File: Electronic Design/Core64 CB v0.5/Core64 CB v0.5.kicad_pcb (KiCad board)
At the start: 2 copper layers, 85 x 85 mm, 36 parts, among them J1 TSM-116-03-T-SV‎, J2 TSM-116-03-T-SV‎, U1 SI7210-B-01, U2 SI7210-B-02, U3 SI7210-B-03, U4 SI7210-B-04, U5 LTR-329ALS-01, U6 TS3A4751PWR, U7 TS3A4751PWR, X1 SFH11-NBPC-D03-ST-BK

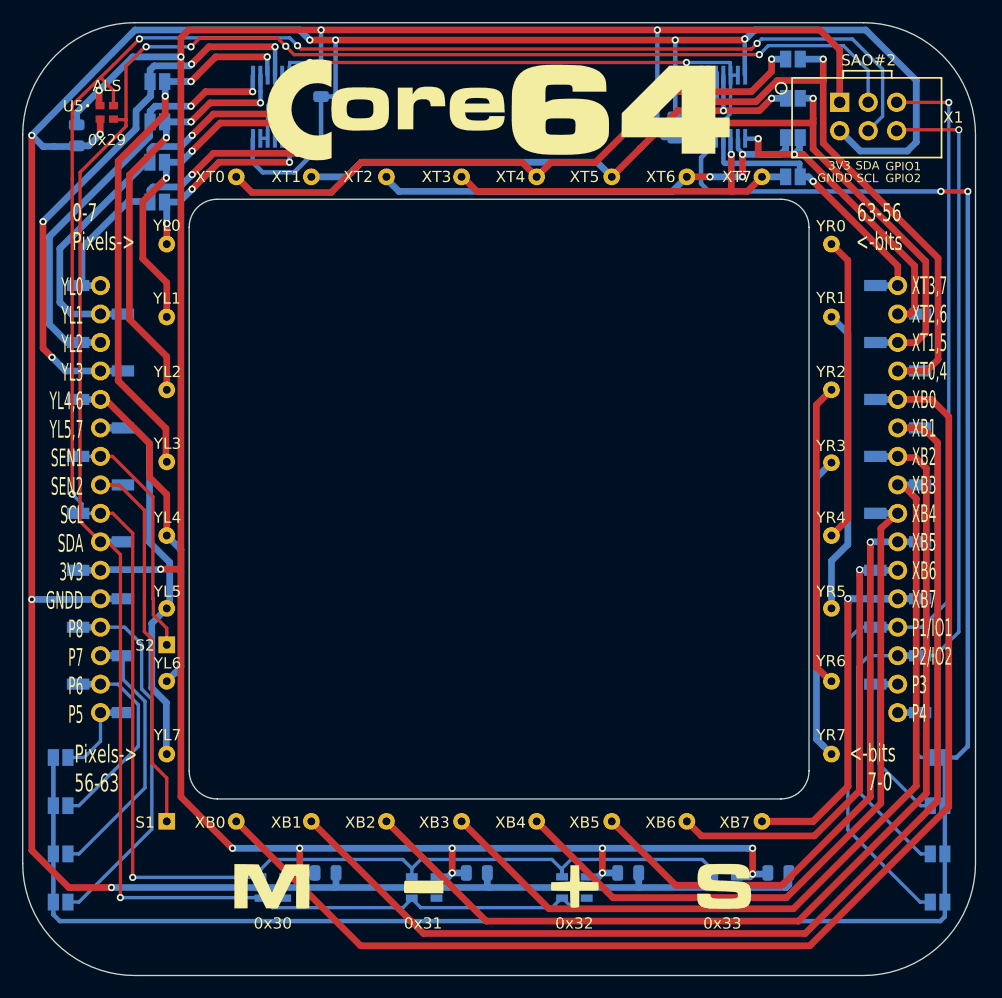
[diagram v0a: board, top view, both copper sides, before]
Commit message: Core board redline refinement
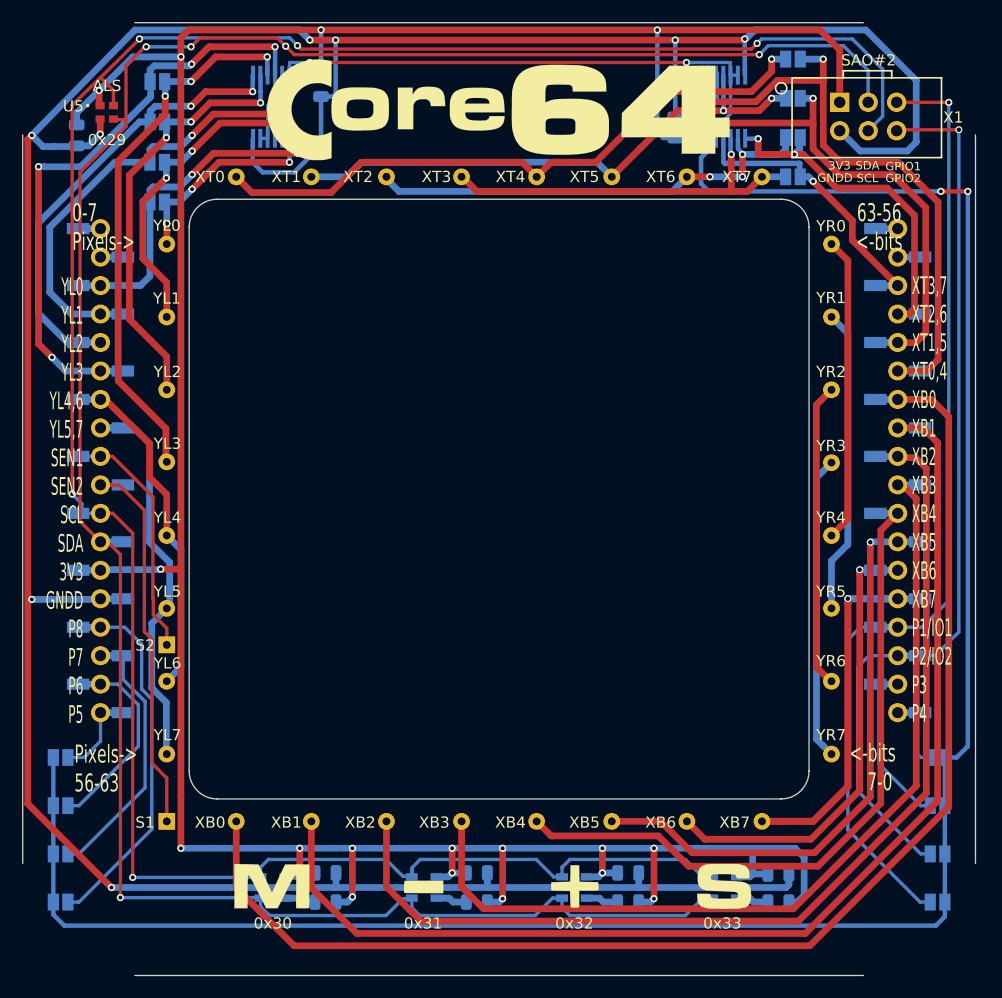
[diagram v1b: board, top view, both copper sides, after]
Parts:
- added R1: 10K, Resistor_SMD:R_0805_2012Metric, B.Cu at (-15.5, 36.0)
- added R2: 10K, Resistor_SMD:R_0805_2012Metric, B.Cu at (-1.99, 36.0)
- added R3: 10K, Resistor_SMD:R_0805_2012Metric, B.Cu at (11.5, 36.0)
- added R4: 10K, Resistor_SMD:R_0805_2012Metric, B.Cu at (24.9, 36.0)
- C5: value 1uF -> 0.1uF
- J1, J2: value TSM-116-03-T-SV‎ -> Digi-Key 77311-420-36LF-ND; footprint Connector_PinHeader_2.54mm:PinHeader_1x16_P2.54mm_Vertical_SMD_and_TH_Pin1Right -> Connector_PinHeader_2.54mm:PinHeader_1x18_P2.54mm_Vertical_SMD_and_TH_Pin1Right
- moved J1 5.08 mm to (-35.6, -5.08)
- moved J2 5.08 mm to (35.6, -5.08)
- moved C4 0.10 mm to (24.9, 33.5)
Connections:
- J1 pad 1: H_YL0 -> Net-(J1-Pad1)
- J1 pad 10: I2C_DATA -> SENSE1
- J1 pad 11: 3V3_800mA -> I2C_CLOCK
- J1 pad 12: GNDD -> I2C_DATA
- J1 pad 13: PLANE_8 -> 3V3_800mA
- J1 pad 14: PLANE_7 -> GNDD
- J1 pad 15: PLANE_6 -> PLANE_8
- J1 pad 16: PLANE_5 -> PLANE_7
- J1 pad 2: H_YL1 -> Net-(J1-Pad2)
- J1 pad 3: H_YL2 -> H_YL0
- J1 pad 4: H_YL3 -> H_YL1
- J1 pad 5: YL4 -> H_YL2
- J1 pad 6: YL5 -> H_YL3
- J1 pad 7: SENSE2 -> YL4
- J1 pad 8: SENSE1 -> YL5
- J1 pad 9: I2C_CLOCK -> SENSE2
- J2 pad 1: H_XT3-7 -> Net-(J2-Pad1)
- J2 pad 10: XB5 -> XB3
- J2 pad 11: XB6 -> XB4
- J2 pad 12: XB7 -> XB5
- J2 pad 13: PLANE_1 -> XB6
- J2 pad 14: PLANE_2 -> XB7
- J2 pad 15: PLANE_3 -> PLANE_1
- J2 pad 16: PLANE_4 -> PLANE_2
- J2 pad 2: H_XT2-6 -> Net-(J2-Pad2)
- J2 pad 3: H_XT1-5 -> H_XT3-7
- J2 pad 4: H_XT0-4 -> H_XT2-6
- J2 pad 5: XB0 -> H_XT1-5
- J2 pad 6: XB1 -> H_XT0-4
- J2 pad 7: XB2 -> XB0
- J2 pad 8: XB3 -> XB1
- J2 pad 9: XB4 -> XB2
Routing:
- net 3V3_800mA: track 248.0 -> 278.6 mm, vias 14 -> 18
- net XB1: track 102.7 -> 106.2 mm
- net XB0: track 114.9 -> 118.4 mm
- net XB2: track 90.2 -> 93.6 mm
- net XB3: track 77.8 -> 81.2 mm
- net I2C_DATA: track 207.5 -> 210.6 mm
- net H_XT0-4: track 53.2 -> 56.2 mm
- net Net-(R3-Pad2): track 0.00 -> 2.91 mm
- net Net-(R4-Pad2): track 0.00 -> 2.91 mm
- net H_XT1-5: track 44.9 -> 47.7 mm
- net Net-(R1-Pad2): track 0.00 -> 2.81 mm
- net Net-(R2-Pad2): track 0.00 -> 2.81 mm
- net H_YL1: track 38.4 -> 41.1 mm
- net H_XT2-6: track 29.4 -> 32.0 mm
- net H_YL3: track 51.1 -> 53.6 mm
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
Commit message: Update core grid to 6.75mm square
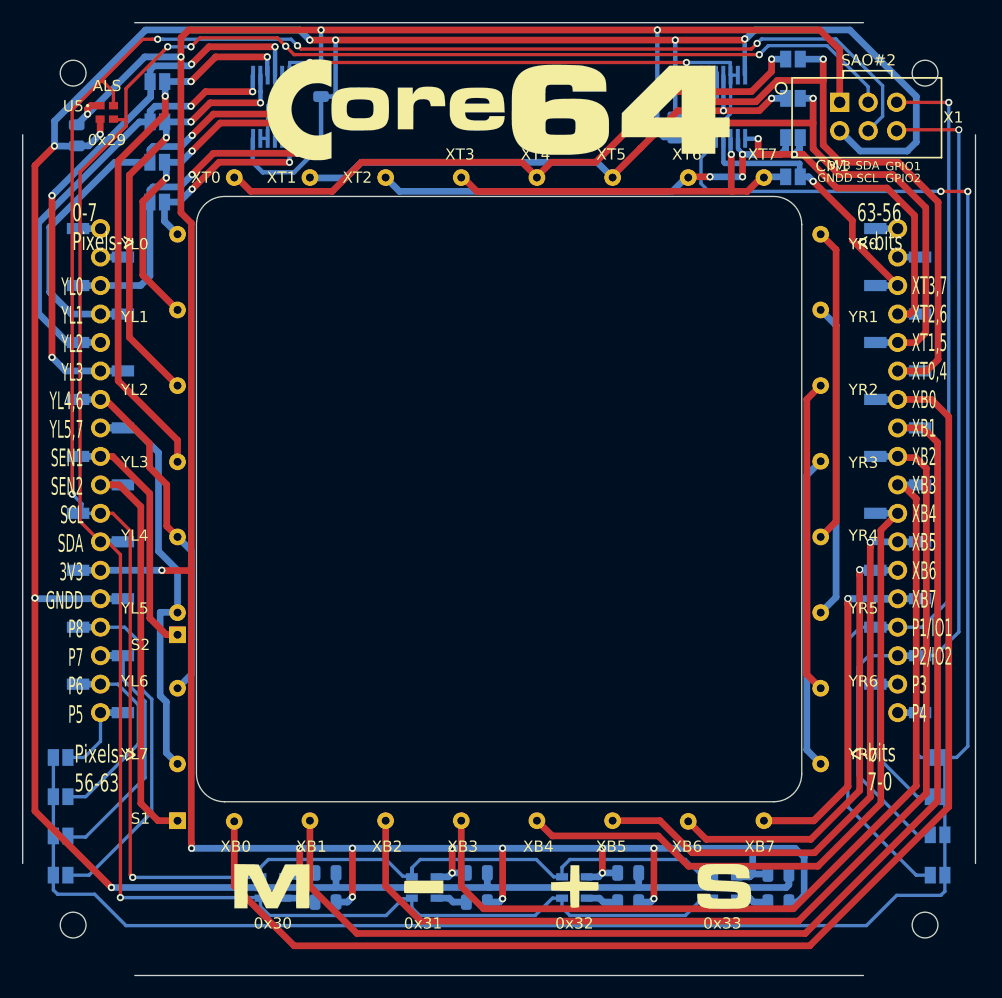
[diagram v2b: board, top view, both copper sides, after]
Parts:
- CM1: footprint Core_Memory_8x8_Array:core_64_x6.7_y6.5mm_v0.3_front_facing -> Core_Memory_8x8_Array:core_64_6.75mm_square_v0.5_front_facing
- moved JP16 2.40 mm to (-39.1, 33.5)
- moved JP9 2.40 mm to (39.1, 33.5)
- moved JP10 1.70 mm to (39.1, 29.9)
- moved JP15 1.60 mm to (-39.1, 30.1)
- moved JP11 0.80 mm to (39.1, 26.6)
- moved JP14 0.80 mm to (-39.1, 26.6)
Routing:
- net GNDD: track 281.0 -> 276.5 mm
- net H_YL3: track 53.6 -> 50.4 mm
- net ENABLE: track 245.4 -> 242.8 mm
- net PLANE_1: track 88.5 -> 86.3 mm
- net YL5: track 36.3 -> 38.4 mm
- net I2C_DATA: track 210.6 -> 208.6 mm
- net PLANE_8: track 35.0 -> 33.1 mm
- net PLANE_2: track 84.2 -> 82.7 mm
- net I2C_CLOCK: track 216.1 -> 214.7 mm
- net SENSE1: track 36.2 -> 37.5 mm
- net PLANE_7: track 26.1 -> 24.8 mm
- net YL4: track 30.5 -> 31.5 mm
- net Net-(CM1-Pad10): track 27.2 -> 28.1 mm
- net Net-(CM1-Pad13): track 27.2 -> 28.1 mm
- net Net-(CM1-Pad12): track 27.1 -> 28.0 mm
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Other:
- outline, holes or cut-outs redrawn
- board text added: "CORE BOARD V0.5 2021-02-15 ANDY GEPPERT WWW.MACHINEIDEAS.COM"
- board text added: "www.Core64.io"
- board text removed: "CORE BOARD V0.4 2020-08-22 ANDY GEPPERT"
- board text removed: "Core64.MachineIdeas.com"

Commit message: Update CB to be compatible with LM V0.1
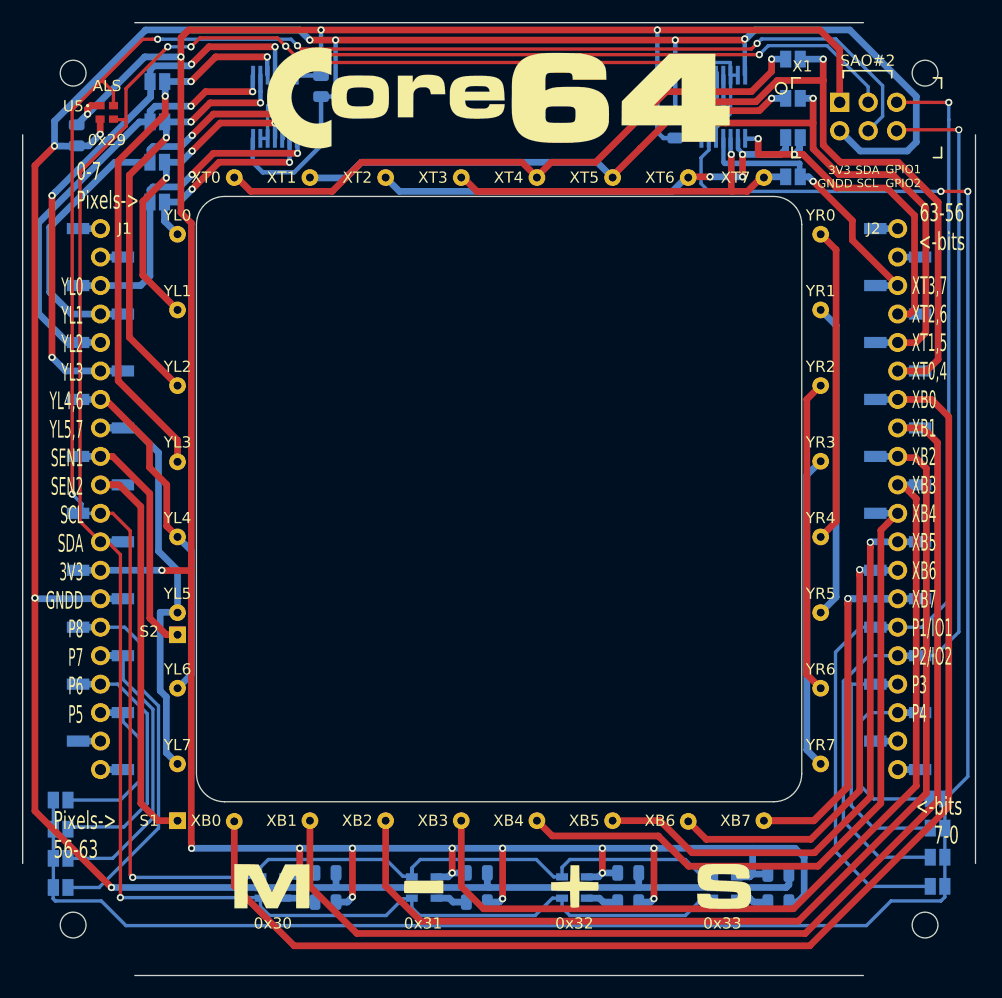
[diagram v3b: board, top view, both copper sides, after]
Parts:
- J1, J2: footprint Connector_PinHeader_2.54mm:PinHeader_1x18_P2.54mm_Vertical_SMD_and_TH_Pin1Right -> Connector_PinHeader_2.54mm:PinHeader_1x20_P2.54mm_Vertical_SMD_and_TH_Pin1Right
- moved JP13 3.80 mm to (-39.1, 26.9)
- moved JP12 3.70 mm to (39.1, 26.8)
- moved JP14 2.90 mm to (-39.1, 29.4)
- moved JP11 2.80 mm to (39.1, 29.4)
- moved JP10 2.00 mm to (39.1, 31.9)
- moved JP15 2.00 mm to (-39.1, 32.0)
- moved JP16 1.10 mm to (-39.1, 34.6)
- moved L1 1.06 mm to (1.81, -35.8)
- moved JP9 1.00 mm to (39.1, 34.5)
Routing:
- net PLANE_4: track 8.62 -> 19.9 mm
- net PLANE_3: track 16.2 -> 24.8 mm
- net PLANE_5: track 8.18 -> 15.9 mm
- net PLANE_6: track 18.0 -> 23.3 mm
- net PLANE_2: track 82.7 -> 87.8 mm
- net PLANE_1: track 86.3 -> 90.6 mm
- net PLANE_7: track 24.8 -> 28.7 mm
- net ENABLE: track 242.8 -> 239.1 mm
- net PLANE_8: track 33.1 -> 35.3 mm
- net Net-(J2-Pad20): track 0.00 -> 2.00 mm
- net Net-(J2-Pad19): track 0.00 -> 2.00 mm
- net Net-(J1-Pad20): track 0.00 -> 2.00 mm
- net Net-(J1-Pad19): track 0.00 -> 2.00 mm
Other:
- board text added: "J1"
- board text added: "J2"
- board text added: "X1"

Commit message: Complete draft V0.5 Core Board changes, new ALS, hall switches
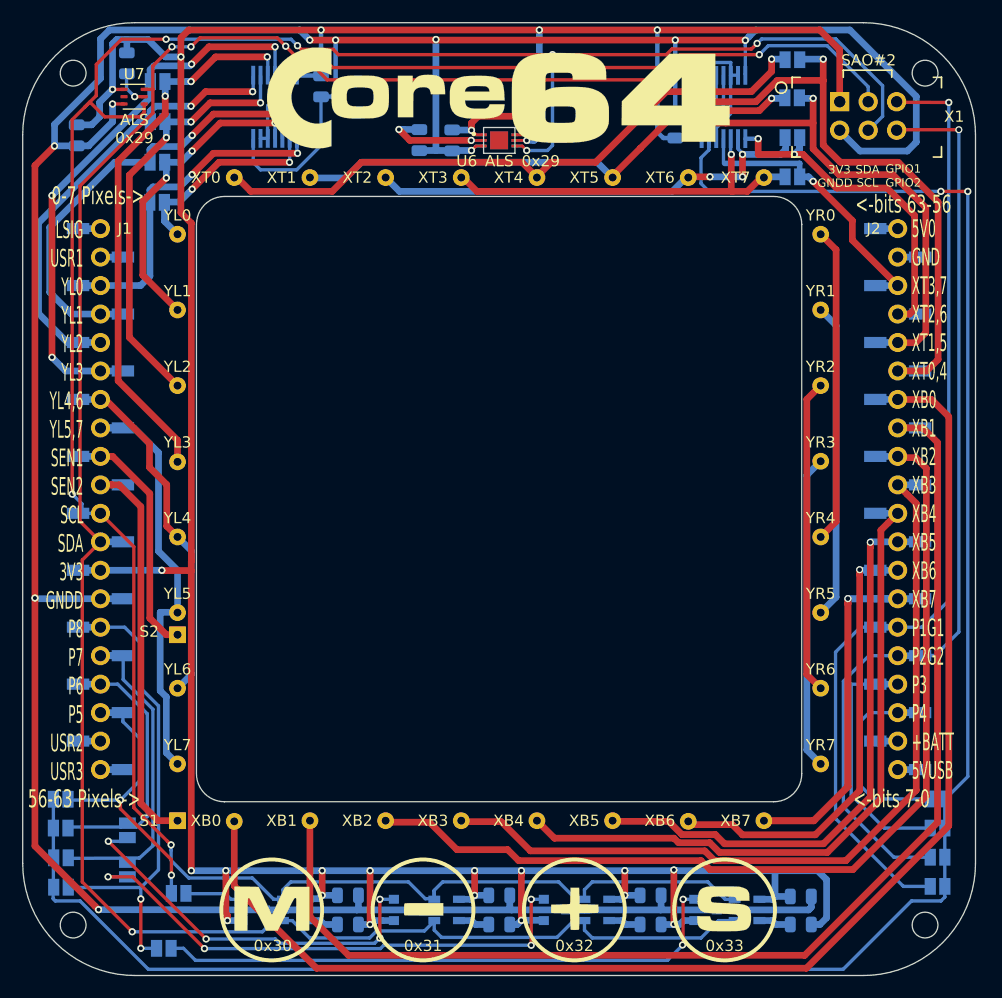
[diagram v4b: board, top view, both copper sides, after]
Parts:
- removed C6: 0.1uF, Capacitor_SMD:C_0805_2012Metric
- added C8: 0.1uF, Capacitor_SMD:C_0805_2012Metric, B.Cu at (-15.9, -36.8)
- added C9: 0.1uF, Capacitor_SMD:C_0805_2012Metric, B.Cu at (15.7, -33.1)
- added JP21: SolderJumper_2_Open, Jumper:SolderJumper-2_P1.3mm_Open_Pad1.0x1.5mm, B.Cu at (-28.6, 35.2)
- added JP22: SolderJumper_2_Open, Jumper:SolderJumper-2_P1.3mm_Open_Pad1.0x1.5mm, B.Cu at (-33.2, 29.6)
- added JP23: SolderJumper_2_Open, Jumper:SolderJumper-2_P1.3mm_Open_Pad1.0x1.5mm, B.Cu at (-33.2, 33.0)
- added JP24: SolderJumper_2_Open, Jumper:SolderJumper-2_P1.3mm_Open_Pad1.0x1.5mm, B.Cu at (-29.9, 40.1)
- added R5: 0, Resistor_SMD:R_0805_2012Metric, B.Cu at (-7.11, -32.0)
- added R7: 10K, Resistor_SMD:R_0805_2012Metric, B.Cu at (-33.2, -38.9)
- added U11: SM353LT, Package_TO_SOT_SMD:SOT-23, B.Cu at (-21.9, 36.6)
- added U12: SM353LT, Package_TO_SOT_SMD:SOT-23, B.Cu at (-8.38, 36.6)
- added U13: SM353LT, Package_TO_SOT_SMD:SOT-23, B.Cu at (4.99, 36.6)
- added U14: SM353LT, Package_TO_SOT_SMD:SOT-23, B.Cu at (18.4, 36.6)
- added U8: TS3A4751PWR, TI_TS3A4751PWR:TS3A4751PWR, B.Cu at (-20.0, -35.0)
- added U9: TS3A4751PWR, TI_TS3A4751PWR:TS3A4751PWR, B.Cu at (20.0, -35.0)
- JP1, JP2, JP3, JP4, JP5, JP6, JP7, JP8: value SolderJumper_2_Bridged -> SolderJumper_2_Open
- JP10, JP11, JP12, JP13, JP14, JP15, JP16, JP9: value SolderJumper_2_Open -> SolderJumper_2_Bridged
- U5: value LTR-329ALS-01 -> BH1730FVC; footprint LiteOn_LTR-329ALS:LTR-329ALS-01 -> ALS_BH1730:BH1730-backside; moved to B.Cu
- U6: value TS3A4751PWR -> BH1730FVC; footprint TI_TS3A4751PWR:TS3A4751PWR -> ALS_BH1730:REG_BD00IC0WHFV-GTR; moved to F.Cu
- U7: value TS3A4751PWR -> LTR-303ALS-01; footprint TI_TS3A4751PWR:TS3A4751PWR -> OptoDevice:Lite-On_LTR-303ALS-01; moved to F.Cu
- moved JP4 94.6 mm to (39.1, 26.8)
- moved JP12 94.5 mm to (-30.5, -37.2)
- moved JP3 93.9 mm to (39.1, 29.4)
- moved JP11 93.9 mm to (-30.5, -33.7)
- moved JP2 93.2 mm to (39.1, 31.9)
- moved JP10 93.2 mm to (-30.5, -30.1)
- moved JP5 92.9 mm to (-39.1, 26.8)
- moved JP13 92.9 mm to (26.2, -39.2)
- moved JP1 92.6 mm to (39.1, 34.5)
- moved JP9 92.6 mm to (-30.5, -26.5)
- moved JP14 92.3 mm to (26.1, -35.8)
- moved JP6 92.2 mm to (-39.1, 29.4)
- moved JP15 91.6 mm to (26.2, -32.2)
- moved JP7 91.6 mm to (-39.1, 32.0)
- moved JP16 91.0 mm to (26.2, -28.8)
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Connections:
- JP1 pad 1: H_YL0 -> PLANE_1
- JP1 pad 2: YL0 -> ENABLE
- JP10 pad 1: PLANE_2 -> H_YL1
- JP10 pad 2: ENABLE -> YL1
- JP11 pad 1: PLANE_3 -> H_YL2
- JP11 pad 2: ENABLE -> YL2
- JP12 pad 1: PLANE_4 -> H_YL3
- JP12 pad 2: ENABLE -> YL3
- JP13 pad 1: PLANE_5 -> H_XT0-4
- JP13 pad 2: ENABLE -> XT0-4
- JP14 pad 1: PLANE_6 -> H_XT1-5
- JP14 pad 2: ENABLE -> XT1-5
- JP15 pad 1: PLANE_7 -> H_XT2-6
- JP15 pad 2: ENABLE -> XT2-6
- JP16 pad 1: PLANE_8 -> H_XT3-7
- JP16 pad 2: ENABLE -> XT3-7
- JP2 pad 1: H_YL1 -> PLANE_2
- JP2 pad 2: YL1 -> ENABLE
- JP3 pad 1: H_YL2 -> PLANE_3
- JP3 pad 2: YL2 -> ENABLE
- JP4 pad 1: H_YL3 -> PLANE_4
- JP4 pad 2: YL3 -> ENABLE
- JP5 pad 1: H_XT0-4 -> PLANE_5
- JP5 pad 2: XT0-4 -> ENABLE
- JP6 pad 1: H_XT1-5 -> PLANE_6
- JP6 pad 2: XT1-5 -> ENABLE
- JP7 pad 1: H_XT2-6 -> PLANE_7
- JP7 pad 2: XT2-6 -> ENABLE
- JP8 pad 1: H_XT3-7 -> PLANE_8
- JP8 pad 2: XT3-7 -> ENABLE
- JP9 pad 1: PLANE_1 -> H_YL0
- JP9 pad 2: ENABLE -> YL0
- U5 pad 2: GNDD -> ALS_INT
- U5 pad 3: I2C_DATA -> GNDD
- U6 pad 1: H_YL0 -> 3V3_800mA
- U6 pad 2: YL0 -> ALS_INT
- U6 pad 3: H_YL1 -> GNDD
- U6 pad 4: YL1 -> I2C_CLOCK
- U6 pad 5: ENABLE -> 3V3_800mA
- U6 pad 6: ENABLE -> I2C_DATA
- U6 pad 7: GNDD -> (no net)
- U7 pad 1: H_XT0-4 -> 3V3_800mA
- U7 pad 2: XT0-4 -> Net-(U7-Pad2)
- U7 pad 3: H_XT1-5 -> GNDD
- U7 pad 4: XT1-5 -> I2C_CLOCK
- U7 pad 5: ENABLE -> Net-(R7-Pad2)
- U7 pad 6: ENABLE -> I2C_DATA
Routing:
- net Net-(JP24-Pad2): track 0.00 -> 51.7 mm, vias 0 -> 2
- net Net-(JP23-Pad2): track 0.00 -> 47.5 mm, vias 0 -> 4
- net 3V3_800mA: track 278.5 -> 322.6 mm, vias 18 -> 24
- net Net-(JP22-Pad2): track 0.00 -> 34.7 mm, vias 0 -> 4
- net GNDD: track 276.5 -> 302.9 mm, vias 8 -> 10
- net I2C_CLOCK: track 214.7 -> 232.8 mm, vias 5 -> 7
- net I2C_DATA: track 208.6 -> 222.4 mm, vias 5 -> 7
- net ALS_INT: track 0.00 -> 10.9 mm, vias 0 -> 2
- net PLANE_5: track 15.9 -> 26.2 mm, vias 0 -> 2
- net PLANE_8: track 35.3 -> 44.3 mm, vias 0 -> 2
- net XB3: track 81.3 -> 74.2 mm
- net XB2: track 93.7 -> 86.7 mm
- net Net-(JP21-Pad2): track 0.00 -> 5.21 mm
- net ENABLE: track 239.1 -> 243.7 mm
- net XB1: track 106.1 -> 110.4 mm
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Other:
- outline, holes or cut-outs redrawn
- board text added: "0x29"
- board text added: "56-63 Pixels->"
- board text added: "5V0 GND XT3,7 XT2,6 XT1,5 XT0,4 XB0 XB1 XB2 XB3 XB4 XB5 XB6 XB7 P1G1 P2G2 P3 P4 +BATT 5VUSB"
- board text added: "<-bits 63-56"
- board text added: "ALS"
- board text added: "LSIG USR1 YL0 YL1 YL2 YL3 YL4,6 YL5,7 SEN1 SEN2 SCL SDA 3V3 GNDD P8 P7 P6 P5 USR2 USR3"
- board text removed: "63-56 <-bits"
- board text removed: "IO1 IO2"
- board text removed: "Pixels-> 56-63"
- board text removed: "XT3,7 XT2,6 XT1,5 XT0,4 XB0 XB1 XB2 XB3 XB4 XB5 XB6 XB7 P1 P2 P3 P4"
- board text removed: "XT3,7 XT2,6 XT1,5 XT0,4 XB0 XB1 XB2 XB3 XB4 XB5 XB6 XB7 P1/IO1 P2/IO2 P3 P4"
- board text removed: "YL0 YL1 YL2 YL3 YL4,6 YL5,7 SEN1 SEN2 SCL SDA 3V3 GNDD P8 P7 P6 P5"
